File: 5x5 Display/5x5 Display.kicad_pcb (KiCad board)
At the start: 4 copper layers, 129.5 x 129.5 mm, 86 parts, among them U3 DRV1

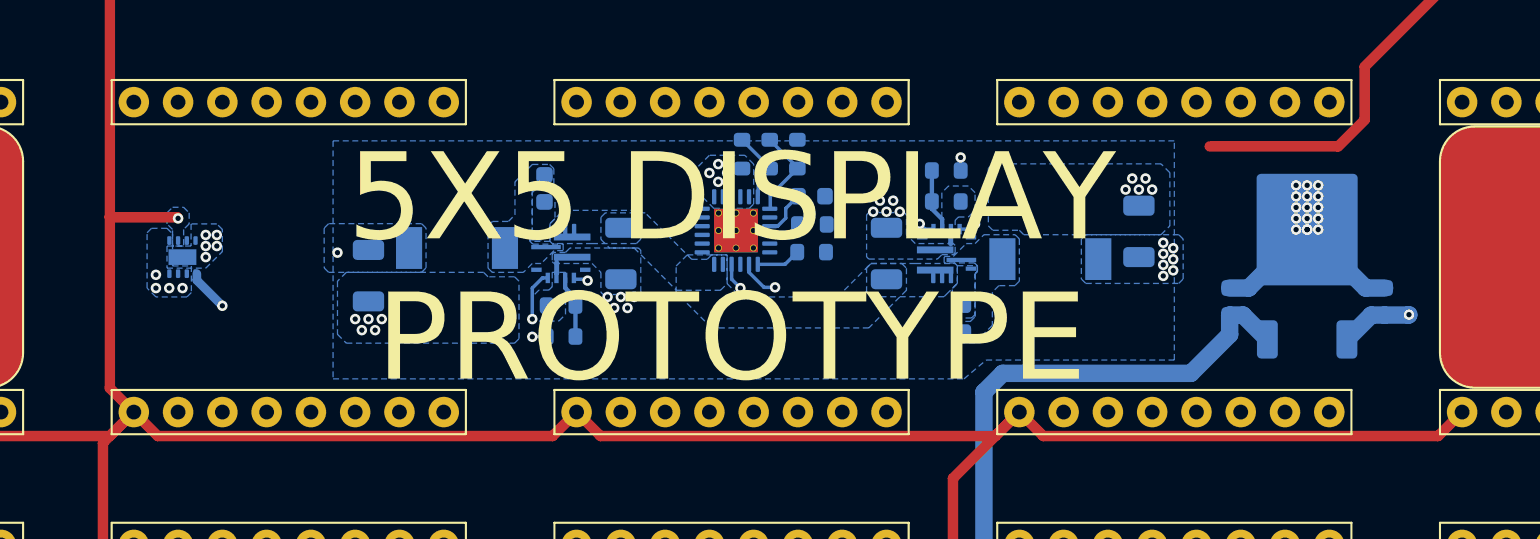
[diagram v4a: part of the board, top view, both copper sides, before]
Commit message: Silkscreens and components
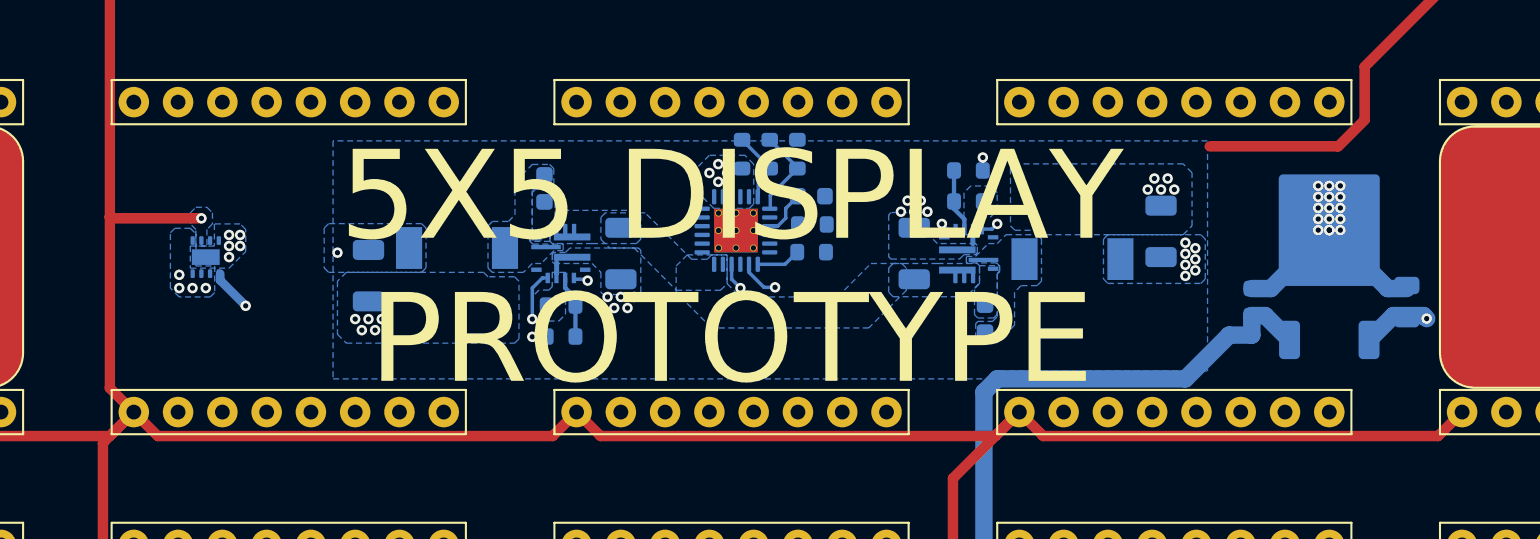
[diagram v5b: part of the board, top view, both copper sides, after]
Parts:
- added G***: LOGO, LOGO, B.Cu at (119.1, 57.1)
- added G***: LOGO, LOGO, B.Cu at (160.7, 106.9)
- added kibuzzard-696556F9: G***, kibuzzard-696556F9, B.Cu at (122.0, 91.9)
- added kibuzzard-69655720: G***, kibuzzard-69655720, B.Cu at (170.2, 91.9)
- added kibuzzard-6965572F: G***, kibuzzard-6965572F, B.Cu at (138.0, 91.9)
- added kibuzzard-6965573A: G***, kibuzzard-6965573A, B.Cu at (154.3, 91.9)
- added kibuzzard-69655742: G***, kibuzzard-69655742, B.Cu at (106.0, 91.9)
- added kibuzzard-6965596D: G***, kibuzzard-6965596D, B.Cu at (103.6, 110.5)
- added kibuzzard-69655B36: G***, kibuzzard-69655B36, B.Cu at (125.2, 110.5)
- added kibuzzard-69658F74: G***, kibuzzard-69658F74, B.Cu at (135.9, 137.9)
- added kibuzzard-69658FBF: G***, kibuzzard-69658FBF, B.Cu at (135.9, 32.3)
- added kibuzzard-69658FCE: G***, kibuzzard-69658FCE, B.Cu at (83.1, 85.1)
- added kibuzzard-69658FDE: G***, kibuzzard-69658FDE, B.Cu at (188.7, 85.1)
- added kibuzzard-69659724: G***, kibuzzard-69659724, B.Cu at (170.2, 66.7)
- added kibuzzard-6965973E: G***, kibuzzard-6965973E, B.Cu at (101.6, 66.7)
- added kibuzzard-69659941: G***, kibuzzard-69659941, B.Cu at (160.7, 117.5)
- C2, C5: value 30μF -> 30μF ≥28V
- C3, C6: value 0.1μF -> 100nF
- C4, C7: value 30μF -> 30μF ≥10V
- C8: value 0.1μF -> 100nF ≥10V
- C9: value 0.33μF -> 330nF ≥28V; footprint Capacitor_SMD:C_0603_1608Metric -> Capacitor_SMD:C_0805_2012Metric
- R6: value 45Ω -> 68kΩ
- R7, R9: value 10kΩ -> 15kΩ
- R8: value 74kΩ -> 110kΩ
- moved C2 1.59 mm to (146.4, 84.9)
- moved U3 1.34 mm to (105.7, 85.1)
- moved REG3 1.27 mm to (170.2, 84.8)
- moved C9 1.27 mm to (174.6, 87.7)
- moved C8 1.27 mm to (165.7, 87.7)
- moved C3 1.27 mm to (150.4, 88.6)
- moved L1 1.27 mm to (155.4, 85.2)
- moved NT1 1.27 mm to (149.7, 84.0)
- moved R6 1.27 mm to (149.5, 80.1)
- moved R7 1.27 mm to (149.5, 81.9)
- moved REG1 1.27 mm to (149.5, 84.9)
- moved C4 1.27 mm to (160.5, 83.6)
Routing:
- net CLK: track 672.5 -> 673.9 mm
- net CLK_LOW: track 571.4 -> 572.7 mm
- net PGOOD: track 24.2 -> 25.5 mm
- net PG_3V: track 66.2 -> 67.5 mm
- net +5V LED: track 76.2 -> 77.5 mm
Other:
- board text added: "${TITLE} ${COMPANY} REV: ${REVISION} DATE: ${CURRENT_DATE} ORDER: JLCJLCJLC ${}"
- board text added: "5x5 Minibadge Display"
- board text added: "Minibadges: 25 In: 5V - 28V 3.25A Out: 3.3V/5V 6A UVLO/OVP: 4.7V-32V"
- board text added: "Pips801"
